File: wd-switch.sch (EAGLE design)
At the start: 13 parts, among them Q1 BC337, Q2 IRF530, Q3 IRF530

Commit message: * Bohrlöcher xD * kleine Verbesserungen im Platinenlayout
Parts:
- R2: device resistor:R-EU_0207/10 -> resistor:R-EU_0207/7
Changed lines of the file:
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@@
 <part name="PAD1" library="wirepad" deviceset="WIREPAD" device="2,54/1,1"/>
 <part name="LED1" library="led" deviceset="LED" device="5MM"/>
-<part name="R2" library="resistor" deviceset="R-EU_" device="0207/10" value="150R"/>
+<part name="R2" library="resistor" deviceset="R-EU_" device="0207/7" value="150R"/>
 <part name="GND2" library="supply1" deviceset="GND" device=""/>
 <part name="C1" library="resistor" deviceset="CPOL-EU" device="E3.5-8"/>

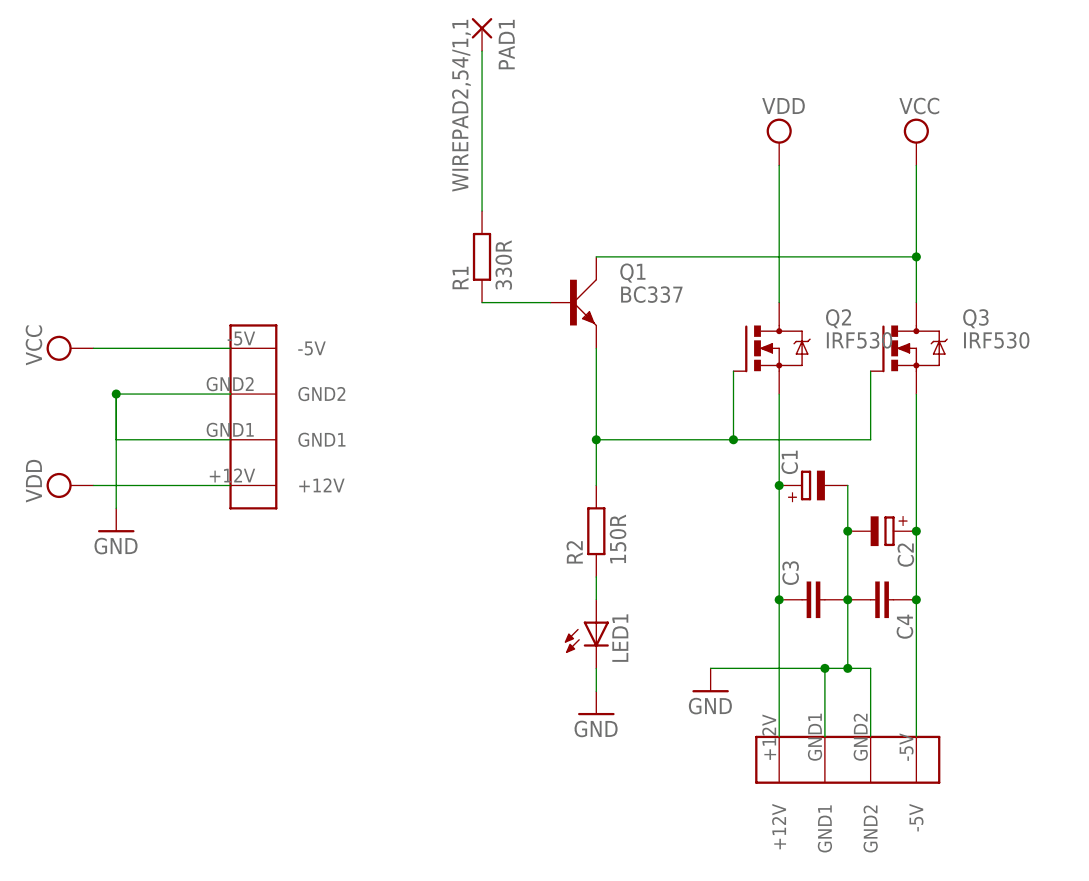
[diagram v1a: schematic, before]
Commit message: Pinheaders für statische Schalterstellung
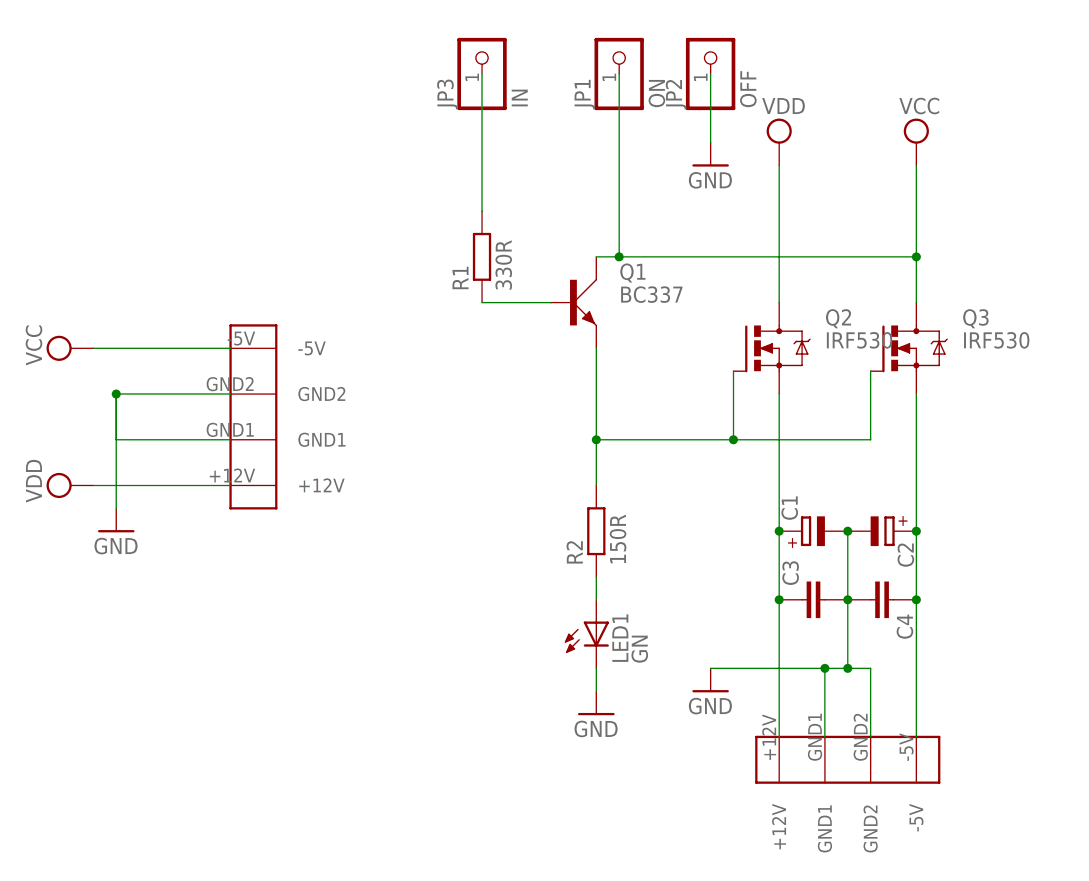
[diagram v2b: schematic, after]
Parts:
- removed PAD1: WIREPAD2,54/1,1, wirepad:WIREPAD2,54/1,1
- added JP1: ON, pinhead:PINHD-1X1
- added JP2: OFF, pinhead:PINHD-1X1
- added JP3: IN, pinhead:PINHD-1X1
- LED1: value (none) -> GN
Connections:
- net GND: now also JP2.1
- net N$5: now also JP3.1; no longer PAD1.P
- net VCC: now also JP1.1
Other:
- moved on the sheet: C1
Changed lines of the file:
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@@
 <part name="U$2" library="n39" deviceset="PSW_5" device=""/>
 <part name="R1" library="resistor" deviceset="R-EU_" device="0207/10" value="330R"/>
-<part name="PAD1" library="wirepad" deviceset="WIREPAD" device="2,54/1,1"/>
-<part name="LED1" library="led" deviceset="LED" device="5MM"/>
+<part name="LED1" library="led" deviceset="LED" device="5MM" value="GN"/>
 <part name="R2" library="resistor" deviceset="R-EU_" device="0207/7" value="150R"/>
 <part name="GND2" library="supply1" deviceset="GND" device=""/>
@@
 <part name="C3" library="resistor" deviceset="C-EU" device="025-024X044"/>
 <part name="C4" library="resistor" deviceset="C-EU" device="025-024X044"/>
+<part name="JP1" library="pinhead" deviceset="PINHD-1X1" device="" value="ON"/>
+<part name="JP2" library="pinhead" deviceset="PINHD-1X1" device="" value="OFF"/>
+<part name="GND3" library="supply1" deviceset="GND" device=""/>
+<part name="JP3" library="pinhead" deviceset="PINHD-1X1" device="" value="IN"/>
 </parts>
 <sheets>
@@
 <instance part="U$2" gate="G$1" x="86.36" y="-15.24"/>
 <instance part="R1" gate="G$1" x="45.72" y="38.1" rot="R90"/>
-<instance part="PAD1" gate="G$1" x="45.72" y="63.5" rot="R270"/>
 <instance part="LED1" gate="G$1" x="58.42" y="-2.54"/>
 <instance part="R2" gate="G$1" x="58.42" y="7.62" rot="R90"/>
 <instance part="GND2" gate="1" x="58.42" y="-12.7"/>
-<instance part="C1" gate="G$1" x="81.28" y="12.7" rot="R90"/>
+<instance part="C1" gate="G$1" x="81.28" y="7.62" rot="R90"/>
 <instance part="C2" gate="G$1" x="91.44" y="7.62" rot="R270"/>
 <instance part="C3" gate="G$1" x="81.28" y="0" rot="R90"/>
 <instance part="C4" gate="G$1" x="91.44" y="0" rot="R270"/>
+<instance part="JP1" gate="G$1" x="60.96" y="60.96" rot="R90"/>
+<instance part="JP2" gate="G$1" x="71.12" y="60.96" rot="R90"/>
+<instance part="GND3" gate="1" x="71.12" y="48.26"/>
+<instance part="JP3" gate="G$1" x="45.72" y="60.96" rot="R90"/>
 </instances>
 <busses>
@@
 <pinref part="Q1" gate="1" pin="C"/>
 <wire x1="93.98" y1="38.1" x2="93.98" y2="33.02" width="0.1524" layer="91"/>
-<wire x1="58.42" y1="38.1" x2="93.98" y2="38.1" width="0.1524" layer="91"/>
+<wire x1="58.42" y1="38.1" x2="60.96" y2="38.1" width="0.1524" layer="91"/>
 <junction x="93.98" y="38.1"/>
+<pinref part="JP1" gate="G$1" pin="1"/>
+<wire x1="60.96" y1="38.1" x2="93.98" y2="38.1" width="0.1524" layer="91"/>
+<wire x1="60.96" y1="58.42" x2="60.96" y2="38.1" width="0.1524" layer="91"/>
+<junction x="60.96" y="38.1"/>
 </segment>
 </net>
@@
 <pinref part="C1" gate="G$1" pin="-"/>
 <pinref part="C2" gate="G$1" pin="-"/>
-<wire x1="86.36" y1="12.7" x2="86.36" y2="7.62" width="0.1524" layer="91"/>
 <wire x1="86.36" y1="7.62" x2="86.36" y2="0" width="0.1524" layer="91"/>
 <junction x="86.36" y="7.62"/>
@@
 <pinref part="GND2" gate="1" pin="GND"/>
 <wire x1="58.42" y1="-7.62" x2="58.42" y2="-10.16" width="0.1524" layer="91"/>
+</segment>
+<segment>
+<pinref part="GND3" gate="1" pin="GND"/>
+<pinref part="JP2" gate="G$1" pin="1"/>
+<wire x1="71.12" y1="50.8" x2="71.12" y2="58.42" width="0.1524" layer="91"/>
 </segment>
 </net>
@@
 <pinref part="Q2" gate="G$1" pin="S"/>
 <pinref part="U$2" gate="G$1" pin="+12V"/>
-<wire x1="78.74" y1="22.86" x2="78.74" y2="12.7" width="0.1524" layer="91"/>
+<wire x1="78.74" y1="22.86" x2="78.74" y2="7.62" width="0.1524" layer="91"/>
 <pinref part="C1" gate="G$1" pin="+"/>
-<wire x1="78.74" y1="12.7" x2="78.74" y2="0" width="0.1524" layer="91"/>
-<junction x="78.74" y="12.7"/>
+<wire x1="78.74" y1="7.62" x2="78.74" y2="0" width="0.1524" layer="91"/>
+<junction x="78.74" y="7.62"/>
 <pinref part="C3" gate="G$1" pin="1"/>
 <wire x1="78.74" y1="0" x2="78.74" y2="-15.24" width="0.1524" layer="91"/>
@@
 </segment>
 </net>
-<net name="N$5" class="0">
-<segment>
-<pinref part="R1" gate="G$1" pin="2"/>
-<pinref part="PAD1" gate="G$1" pin="P"/>
-<wire x1="45.72" y1="43.18" x2="45.72" y2="60.96" width="0.1524" layer="91"/>
-</segment>
-</net>
 <net name="N$7" class="0">
 <segment>
@@
 </segment>
 </net>
+<net name="N$5" class="0">
+<segment>
+<pinref part="R1" gate="G$1" pin="2"/>
+<pinref part="JP3" gate="G$1" pin="1"/>
+<wire x1="45.72" y1="43.18" x2="45.72" y2="58.42" width="0.1524" layer="91"/>
+</segment>
+</net>

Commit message: USB-Stromversorgung
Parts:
- added X1: KUSBVX, con-kycon:KUSBVX
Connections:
- net GND: now also X1.4
- net VCC: now also X1.1
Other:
- moved on the sheet: JP3, R1
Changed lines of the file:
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@@
 <part name="GND3" library="supply1" deviceset="GND" device=""/>
 <part name="JP3" library="pinhead" deviceset="PINHD-1X1" device="" value="IN"/>
+<part name="X1" library="con-kycon" deviceset="KUSBVX" device=""/>
+<part name="SUPPLY4" library="supply2" deviceset="VCC" device=""/>
+<part name="GND5" library="supply1" deviceset="GND" device=""/>
 </parts>
 <sheets>
@@
 <instance part="SUPPLY3" gate="G$1" x="78.74" y="50.8"/>
 <instance part="U$2" gate="G$1" x="86.36" y="-15.24"/>
-<instance part="R1" gate="G$1" x="45.72" y="38.1" rot="R90"/>
+<instance part="R1" gate="G$1" x="50.8" y="45.72" rot="R90"/>
 <instance part="LED1" gate="G$1" x="58.42" y="-2.54"/>
 <instance part="R2" gate="G$1" x="58.42" y="7.62" rot="R90"/>
@@
 <instance part="JP2" gate="G$1" x="71.12" y="60.96" rot="R90"/>
 <instance part="GND3" gate="1" x="71.12" y="48.26"/>
-<instance part="JP3" gate="G$1" x="45.72" y="60.96" rot="R90"/>
+<instance part="JP3" gate="G$1" x="50.8" y="60.96" rot="R90"/>
+<instance part="X1" gate="G$1" x="20.32" y="50.8"/>
+<instance part="SUPPLY4" gate="G$1" x="5.08" y="55.88" rot="R90"/>
+<instance part="GND5" gate="1" x="5.08" y="45.72"/>
 </instances>
 <busses>
@@
 <wire x1="60.96" y1="58.42" x2="60.96" y2="38.1" width="0.1524" layer="91"/>
 <junction x="60.96" y="38.1"/>
+</segment>
+<segment>
+<pinref part="SUPPLY4" gate="G$1" pin="VCC"/>
+<pinref part="X1" gate="G$1" pin="1"/>
+<wire x1="7.62" y1="55.88" x2="15.24" y2="55.88" width="0.1524" layer="91"/>
 </segment>
 </net>
@@
 <pinref part="JP2" gate="G$1" pin="1"/>
 <wire x1="71.12" y1="50.8" x2="71.12" y2="58.42" width="0.1524" layer="91"/>
+</segment>
+<segment>
+<pinref part="GND5" gate="1" pin="GND"/>
+<pinref part="X1" gate="G$1" pin="4"/>
+<wire x1="5.08" y1="48.26" x2="15.24" y2="48.26" width="0.1524" layer="91"/>
 </segment>
 </net>
@@
 <pinref part="R1" gate="G$1" pin="1"/>
 <pinref part="Q1" gate="1" pin="B"/>
-<wire x1="45.72" y1="33.02" x2="53.34" y2="33.02" width="0.1524" layer="91"/>
+<wire x1="50.8" y1="40.64" x2="50.8" y2="33.02" width="0.1524" layer="91"/>
+<wire x1="50.8" y1="33.02" x2="53.34" y2="33.02" width="0.1524" layer="91"/>
 </segment>
 </net>
@@
 <pinref part="R1" gate="G$1" pin="2"/>
 <pinref part="JP3" gate="G$1" pin="1"/>
-<wire x1="45.72" y1="43.18" x2="45.72" y2="58.42" width="0.1524" layer="91"/>
+<wire x1="50.8" y1="50.8" x2="50.8" y2="58.42" width="0.1524" layer="91"/>
 </segment>
 </net>

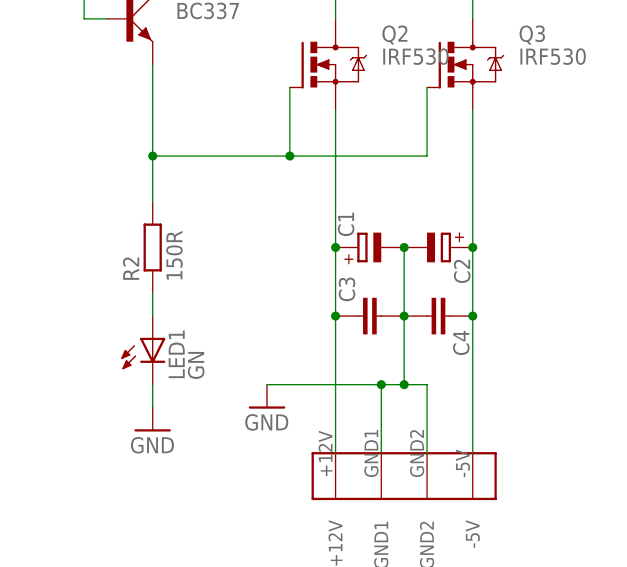
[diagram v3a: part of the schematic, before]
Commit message: Werte für die Kondensatoren angegeben
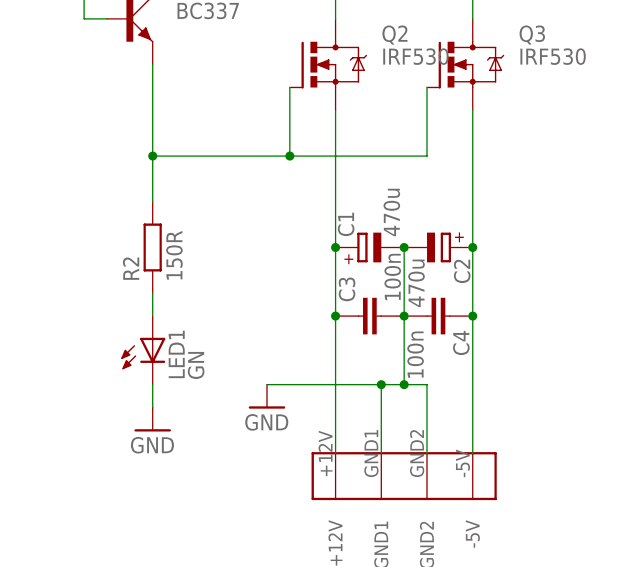
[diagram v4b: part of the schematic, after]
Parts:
- C1, C2: value (none) -> 470u
- C3, C4: value (none) -> 100n
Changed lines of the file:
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@@
 <part name="R2" library="resistor" deviceset="R-EU_" device="0207/7" value="150R"/>
 <part name="GND2" library="supply1" deviceset="GND" device=""/>
-<part name="C1" library="resistor" deviceset="CPOL-EU" device="E3.5-8"/>
-<part name="C2" library="resistor" deviceset="CPOL-EU" device="E3.5-8"/>
-<part name="C3" library="resistor" deviceset="C-EU" device="025-024X044"/>
-<part name="C4" library="resistor" deviceset="C-EU" device="025-024X044"/>
+<part name="C1" library="resistor" deviceset="CPOL-EU" device="E3.5-8" value="470u"/>
+<part name="C2" library="resistor" deviceset="CPOL-EU" device="E3.5-8" value="470u"/>
+<part name="C3" library="resistor" deviceset="C-EU" device="025-024X044" value="100n"/>
+<part name="C4" library="resistor" deviceset="C-EU" device="025-024X044" value="100n"/>
 <part name="JP1" library="pinhead" deviceset="PINHD-1X1" device="" value="ON"/>
 <part name="JP2" library="pinhead" deviceset="PINHD-1X1" device="" value="OFF"/>
